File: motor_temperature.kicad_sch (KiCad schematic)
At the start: 18 parts, among them J1 TBL002A-350-03GR-2OR, J2 TBL002A-350-03GR-2OR, J3 TBL002A-350-03GR-2OR, U1 DRV8870DDA, U2 L9110S, U3 TMP144YFFR, U4 TMP75AIDR

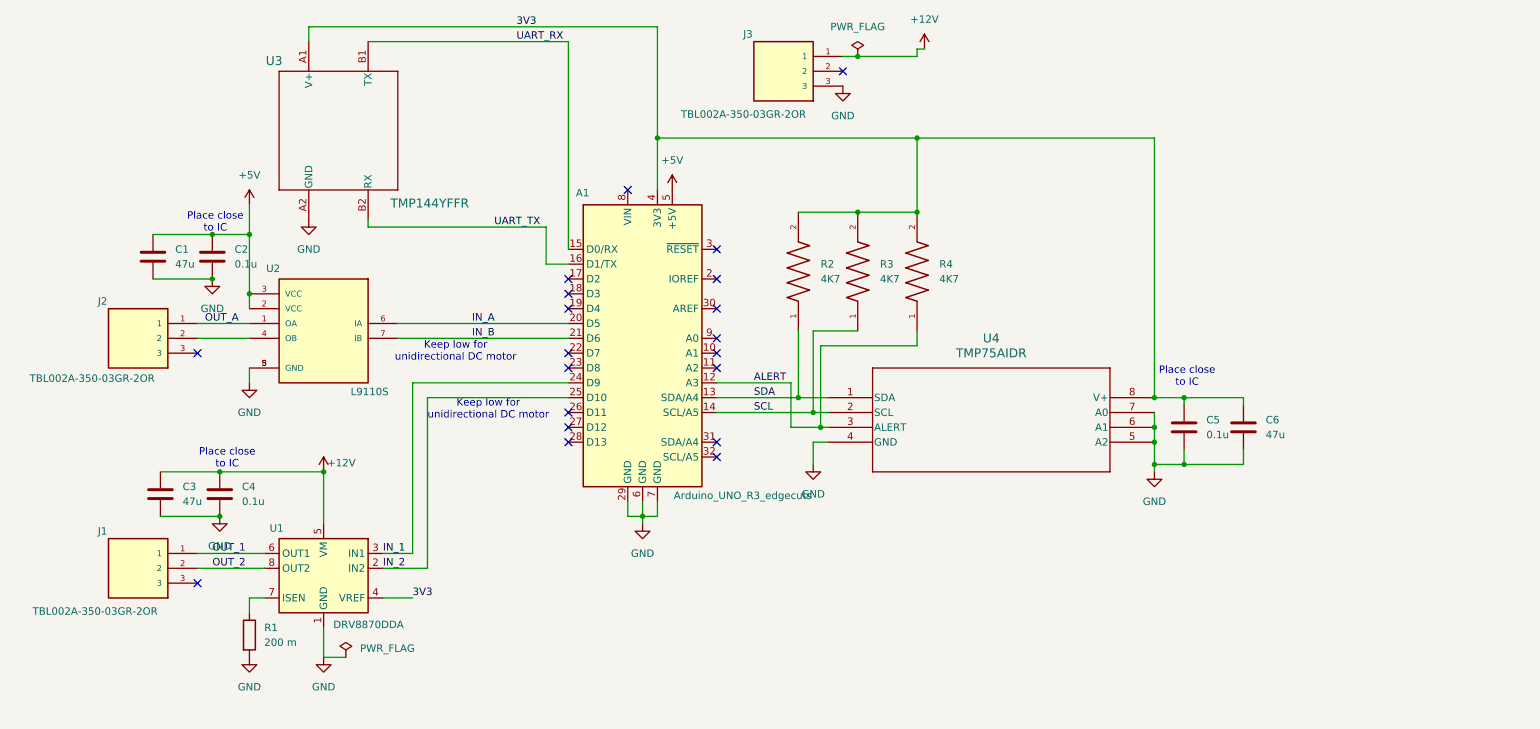
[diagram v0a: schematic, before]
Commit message: Incorporated feedback
1) Flipped Arduino template for shield to correctly match the STM32 Dicovery board. Rerouted the circuit modules.
2) Labeled terminals
3) Removed unnecessary tabs
4) Added trace for Tachometer with 0 Ohm resistor
5) Resolved all DRC issues related to silkscreen and clearance
6) Generated Gerbers, drill files and BOM
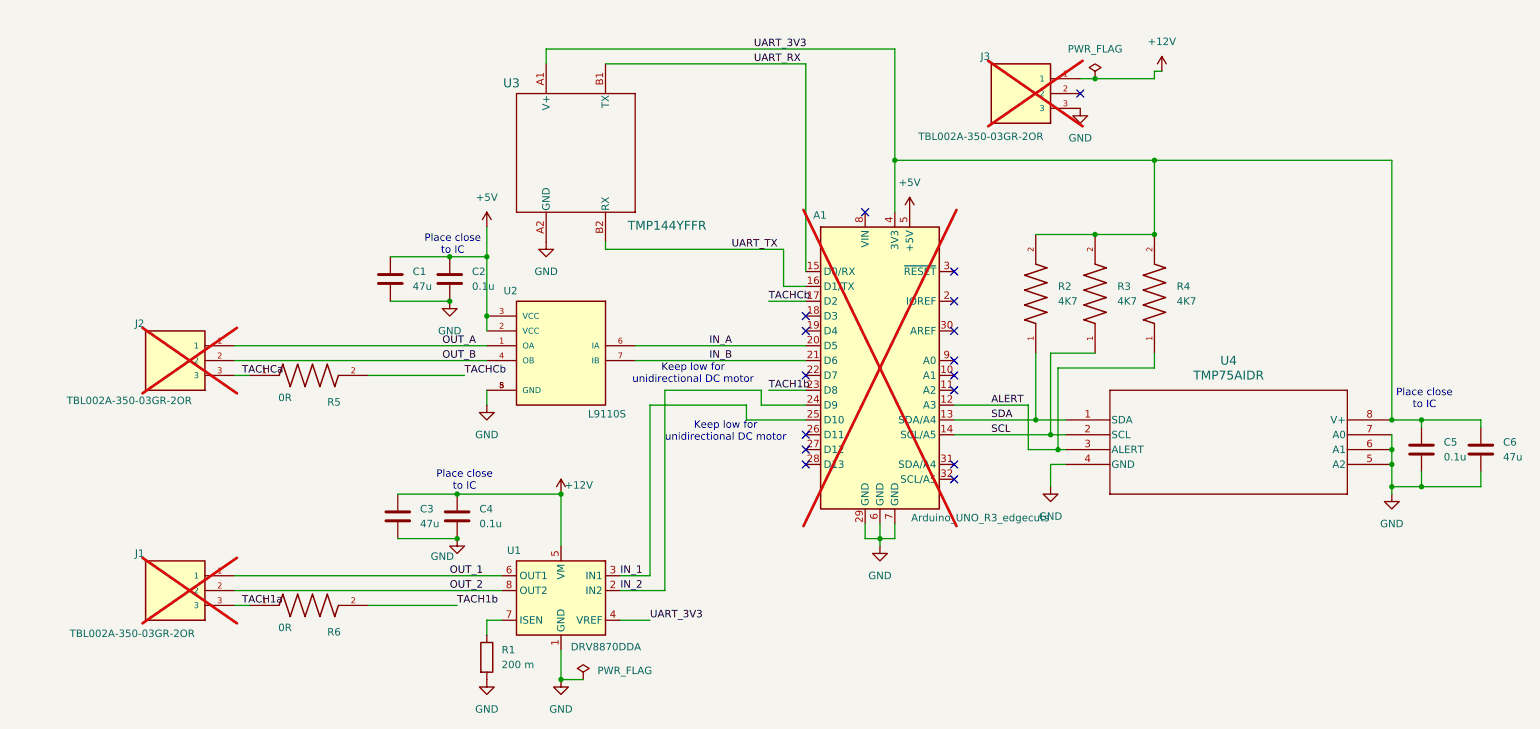
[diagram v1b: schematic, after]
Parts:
- added R5, R6: 0R, 1206W4F0000T5E:RESC3115X65N, symbol 1206W4F0000T5E:1206W4F0000T5E
- A1: footprint Module:Arduino_UNO_R3_edgecuts_withoutcourtyard -> Module:Arduino_UNO_R3_edgecuts_withoutcourtyard_notabs_nosilkscreern; now not fitted
- C1, C3, C6: Jabil_Link1 (none) -> https://jlcpcb.com/partdetail/HRE-CGA1210X5R476M250RT/C6120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; MPN1 (none) -> CGA1210X5R476M250RT; Vendor1 (none) -> HRE
- C2, C4, C5: Jabil_Link1 (none) -> https://jlcpcb.com/partdetail/HRE-CGA0603X7R104K250JT/C6119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; MPN1 (none) -> CGA0603X7R104K250JT; Vendor1 (none) -> HRE
- J1, J2, J3: now not fitted
- R1: Jabil_Link1 (none) -> https://jlcpcb.com/partdetail/21398-0603WAF220LT5E/C20686; MPN1 (none) -> 0603WAF220LT5E; Vendor1 (none) -> UNI-ROYAL(Uniroyal Elec)
- R2, R3, R4: Jabil_Link1 (none) -> https://jlcpcb.com/partdetail/18624-1206W4F4701T5E/C17936; MPN1 (none) -> 1206W4F4701T5E; Vendor1 (none) -> UNI-ROYAL(Uniroyal Elec)
- U1: Jabil_Link1 (none) -> https://jlcpcb.com/partdetail/TexasInstruments-DRV8870DDAR/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; MPN1 (none) -> DRV8870DDAR; Vendor1 (none) -> Texas Instruments
- U2: Description_1 Buck-Boost Switching Regulator IC Positive Adjustable 1V 1 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 -> SOP-8 MOTOR DRIVER ICS ROHS; Jabil_Link1 (none) -> https://jlcpcb.com/partdetail/772196-L9110S/C725793; MPN1 (none) -> L9110S; Vendor1 (none) -> UMW(Youtai Semiconductor Co., Ltd.)
- U3: Jabil_Link1 (none) -> https://jlcpcb.com/partdetail/TexasInstruments-TMP144YFFR/C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; MPN1 (none) -> TMP144YFFR; Vendor1 (none) -> Texas Instruments
- U4: Jabil_Link1 (none) -> https://jlcpcb.com/partdetail/TexasInstruments-TMP75AIDR/C3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; MPN1 (none) -> TMP75AIDR; Vendor1 (none) -> Texas Instruments
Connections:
- net IN_1: now also A1.25 (D10); no longer A1.24 (D9)
- net IN_2: now also A1.24 (D9); no longer A1.25 (D10)
- net OUT_B: now reaches J2.2, U2.4 (OB)
- net TACHCa: now reaches J2.3
- net TACHCa: now also R5.1
- net TACHCb: now reaches A1.17 (D2)
- net TACHCb: now also R5.2
- net TACH1b: now reaches A1.23 (D8)
- net TACH1b: now also R6.2
- net TACH1a: now reaches J1.3
- net TACH1a: now also R6.1
- net 3V3 renamed UART_3V3
- no-connect marks 20 -> 16
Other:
- moved on the sheet: C1, C2, C3, C4, C5, C6, R1, R2, R3, R4, U1, U2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
